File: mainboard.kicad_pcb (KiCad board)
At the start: 2 copper layers, 144 parts, among them IC1 ATXMEGA128A1U-A, J1 USB, K1 X_MIN, K2 X_MAX, K3 Y_MIN, K4 Y_MAX, K5 Z_MIN, K6 Z_MAX, P1 POWER, P10 USART, P11 TH_HB, P12 TH_EX, P13 TH_HO, P14 LCD, P15 STP_Y, P16 STP_E0, P17 STP_X, P18 STP_E1, P19 STP_Z, P2 PDI, P20 EXTR, P21 HIC_0, P22 HEATBED, P23 HIC_1, P24 FAN_0, P25 FAN_1, P26 LOC_0, P27 LOC_1, P28 INTERFACE, P3 GPIO_B, P4 BEEPER, P5 OPEN_COLL_D, P6 12V, P7 5V, P8 3.3V, P9 I2C, Q1 IRL1404, Q2 IRL1404, Q3 IRL1404, Q4 IRL1404, SW1 Y, SW2 E0, SW3 X, SW4 E1, SW5 Z, U1 NE 4558 D SMD, U10 ULN_2003_A, U2 ULN_2003_A, U3 A4988-BO, U4 A4988-BO, U5 A4988-BO, U6 A4988-BO, U7 A4988-BO, U8 MCP14E10, U9 MCP14E10

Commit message: * Changed order of stepper connections to UC to ease PCB routing * Arranged all items in 12x12cm space, ready to route(?)
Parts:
- C10, C11, C2, C4, C5, C6, C7, C8, C9, R1, R2, R21, R22, R23, R24: moved to B.Cu
- P1: footprint Connect:PINHEAD1-6 -> Connect:bornier6
- P11, P12, P13: footprint Connect:PINHEAD1-2 -> 3dp-special:PSS2
- moved P5 319.2 mm to (20.0, 109.5), turned to 270 degrees
- moved U2 308.8 mm to (30.5, 112.5), turned to 270 degrees
- moved C17 238.9 mm to (103.8, 42.8), turned to 90 degrees
- moved P14 230.0 mm to (109.8, 46.8), turned to 270 degrees
- moved R7 219.9 mm to (121.0, 40.5), turned to 90 degrees
- moved RV5 218.5 mm to (110.0, 28.5), turned to 270 degrees
- moved R26 215.6 mm to (48.0, 41.0), turned to 270 degrees
- moved R6 214.9 mm to (118.5, 47.0), turned to 90 degrees
- moved VR1 213.2 mm to (121.0, 46.5), turned to 90 degrees
- moved J1 209.0 mm to (126.5, 30.2), turned to 90 degrees
- moved VR2 209.0 mm to (118.5, 52.5), turned to 90 degrees
- moved R32 206.9 mm to (45.0, 75.0), turned to 90 degrees
- moved SW2 206.4 mm to (129.5, 45.0), turned to 90 degrees
- moved C12 205.1 mm to (121.5, 53.5), turned to 90 degrees
- moved R30 204.1 mm to (45.0, 86.0), turned to 90 degrees
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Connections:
- IC1 pad 56: Y-DIR -> X-STEP
- IC1 pad 57: Z-DIR -> X-EN
- IC1 pad 58: E0-STEP -> Y-DIR
- IC1 pad 59: E1-STEP -> Y-STEP
- IC1 pad 60: X-STEP -> Y-EN
- IC1 pad 61: Y-STEP -> Z-DIR
- IC1 pad 65: E0-EN -> Z-EN
- IC1 pad 66: E1-EN -> E0-DIR
- IC1 pad 67: X-EN -> E0-STEP
- IC1 pad 68: Y-EN -> E0-EN
- IC1 pad 69: Z-EN -> E1-DIR
- IC1 pad 70: E0-DIR -> E1-STEP
- IC1 pad 71: E1-DIR -> E1-EN
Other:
- board text added: "3V3"
- board text added: "E0"
- board text added: "E1"
- board text added: "GND"
- board text added: "HEATSINK"
- board text added: "SCL"
- board text added: "SDA"
- board text added: "STEP_X SETTINGS"
- board text added: "STEP_Y SETTINGS"
- board text added: "TH_EX"
- board text added: "TH_HB"
- board text added: "TH_HO"
- board text added: "VOL"
- board text added: "X"
- board text added: "Y"
- board text added: "Z"

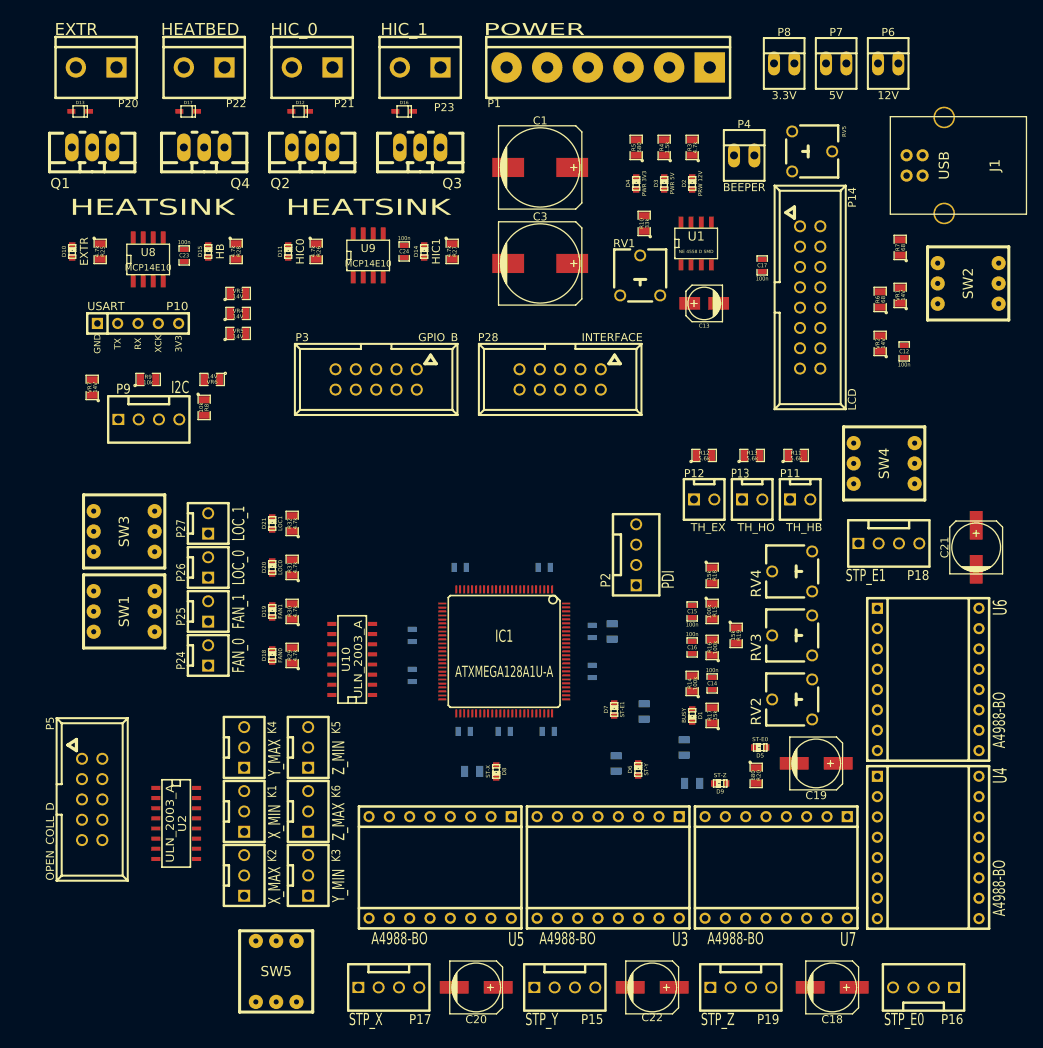
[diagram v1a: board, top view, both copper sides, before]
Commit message: * Schematic: Added decoupling cap for XMega * Schematic: Changed connector pin assignment for easier routing * Board: Changed arrangement of some components * Board: Routed all signal nets. To Do: Power nets.
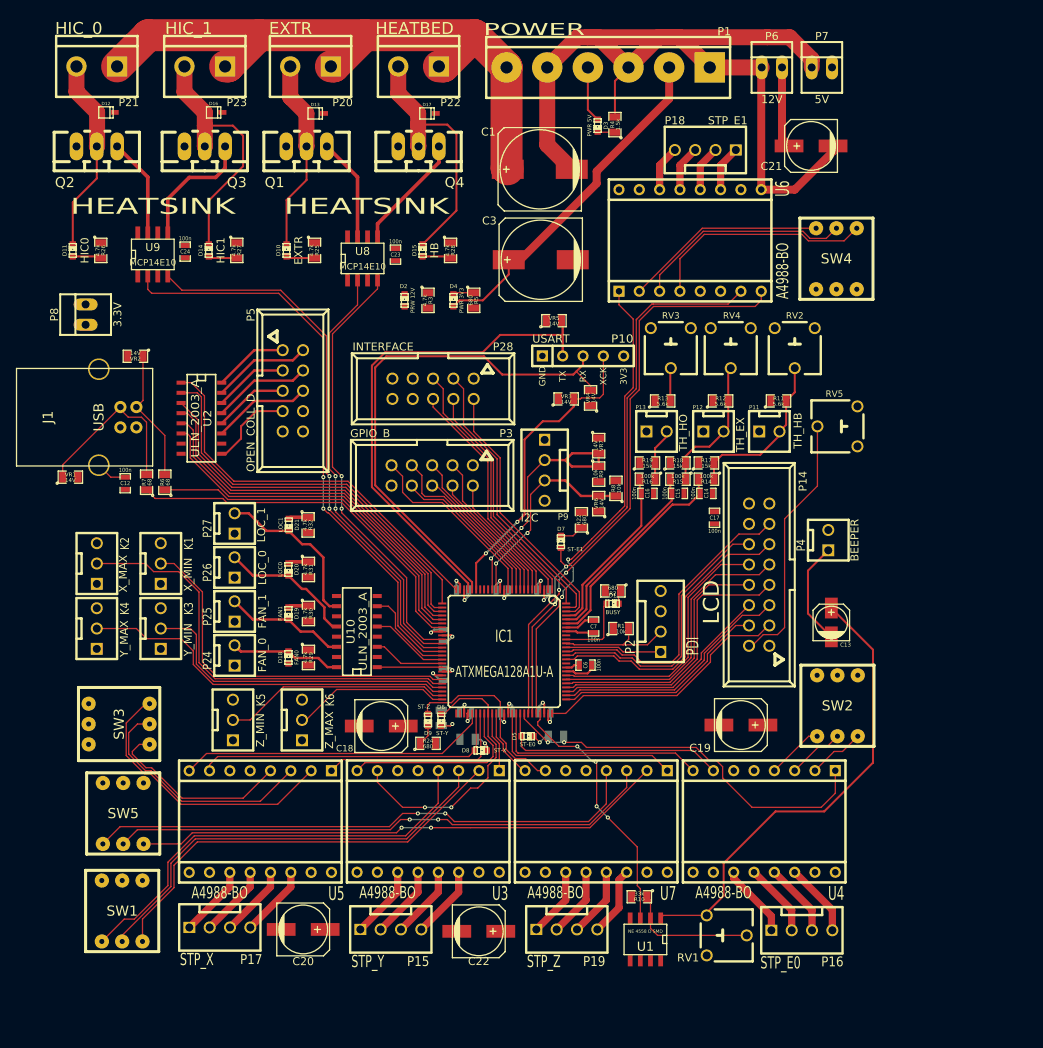
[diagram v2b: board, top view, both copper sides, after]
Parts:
- added C25: 100n, SMD_Packages:SM0603_Capa, B.Cu at (71.2, 83.3)
- C6, C7, R1, R2, R22, R24: moved to F.Cu
- P4: footprint Connect:PINHEAD1-2 -> 3dp-special:PSS2
- R20: moved to B.Cu
- moved J1 110.3 mm to (20.8, 61.7), turned to 270 degrees
- moved VR1 106.2 mm to (17.3, 69.2), turned to 0 degrees
- moved C12 98.8 mm to (24.1, 70.0), turned to 270 degrees
- moved R7 98.7 mm to (26.8, 69.8)
- moved VR2 93.1 mm to (25.4, 54.1), turned to 180 degrees
- moved P8 92.8 mm to (19.2, 48.9), turned to 90 degrees
- moved R6 92.3 mm to (29.1, 69.8)
- moved U1 87.2 mm to (89.2, 127.0), turned to 180 degrees
- moved R10 84.2 mm to (88.4, 121.7), turned to 180 degrees
- moved RV1 83.2 mm to (99.3, 126.5), turned to 270 degrees
- moved C18 65.1 mm to (56.1, 100.3)
- moved VR7 63.7 mm to (83.3, 65.3), turned to 270 degrees
- moved U6 62.4 mm to (94.7, 39.6), turned to 0 degrees
- moved R9 57.5 mm to (83.3, 68.8), turned to 270 degrees
- moved P5 56.9 mm to (45.1, 58.4)
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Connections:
- net Net-(D18-Pad2) renamed /heater-fan-driver/FAN1_OPEM
- net Net-(D19-Pad2) renamed /heater-fan-driver/FAN0_OPEM
- net Net-(D20-Pad2) renamed /heater-fan-driver/LOC1_OPEM
- net Net-(D21-Pad2) renamed /heater-fan-driver/LOC0_OPEM
- IC1 pad 17: /LCD_EN -> Net-(IC1-Pad17)
- IC1 pad 18: /LCD_RS -> Net-(IC1-Pad18)
- IC1 pad 86: Net-(IC1-Pad86) -> /LCD_RW
- IC1 pad 87: Net-(D1-Pad1) -> /LCD_RS
- IC1 pad 88: Net-(IC1-Pad88) -> /LCD_EN
- IC1 pad 91: Net-(IC1-Pad91) -> Net-(D1-Pad1)
- P14 pad 10: /LCD_D1 -> /LCD_D7
- P14 pad 11: /LCD_D0 -> /LCD_RW
- P14 pad 3: GND -> /LCD_D0
- P14 pad 4: /LCD_D7 -> /LCD_D1
- P14 pad 5: /LCD_D6 -> /LCD_D2
- P14 pad 6: /LCD_D5 -> /LCD_D3
- P14 pad 8: /LCD_D3 -> /LCD_D5
- P14 pad 9: /LCD_D2 -> /LCD_D6
- SW1 pad 1: Net-(SW1-Pad1) -> +3.3V
- SW1 pad 2: Net-(SW1-Pad2) -> +3.3V
- SW1 pad 3: Net-(SW1-Pad3) -> +3.3V
- SW1 pad 4: +3.3V -> Net-(SW1-Pad4)
- SW1 pad 5: +3.3V -> Net-(SW1-Pad5)
- SW1 pad 6: +3.3V -> Net-(SW1-Pad6)
- SW2 pad 1: Net-(SW2-Pad1) -> +3.3V
- SW2 pad 2: Net-(SW2-Pad2) -> +3.3V
- SW2 pad 3: Net-(SW2-Pad3) -> +3.3V
- SW2 pad 4: +3.3V -> Net-(SW2-Pad4)
- SW2 pad 5: +3.3V -> Net-(SW2-Pad5)
- SW2 pad 6: +3.3V -> Net-(SW2-Pad6)
- SW3 pad 1: Net-(SW3-Pad1) -> +3.3V
- SW3 pad 2: Net-(SW3-Pad2) -> +3.3V
- SW3 pad 3: Net-(SW3-Pad3) -> +3.3V
- SW3 pad 4: +3.3V -> Net-(SW3-Pad4)
- SW3 pad 5: +3.3V -> Net-(SW3-Pad5)
- SW3 pad 6: +3.3V -> Net-(SW3-Pad6)
- SW4 pad 1: Net-(SW4-Pad1) -> +3.3V
- SW4 pad 2: Net-(SW4-Pad2) -> +3.3V
- SW4 pad 3: Net-(SW4-Pad3) -> +3.3V
- SW4 pad 4: +3.3V -> Net-(SW4-Pad4)
- SW4 pad 5: +3.3V -> Net-(SW4-Pad5)
- SW4 pad 6: +3.3V -> Net-(SW4-Pad6)
- SW5 pad 1: Net-(SW5-Pad1) -> +3.3V
- SW5 pad 2: Net-(SW5-Pad2) -> +3.3V
- SW5 pad 3: Net-(SW5-Pad3) -> +3.3V
- SW5 pad 4: +3.3V -> Net-(SW5-Pad4)
- SW5 pad 5: +3.3V -> Net-(SW5-Pad5)
- SW5 pad 6: +3.3V -> Net-(SW5-Pad6)
- U10 pad 1: /heater-fan-driver/IN_FAN_0 -> /heater-fan-driver/IN_FAN_1
- U10 pad 3: /heater-fan-driver/IN_FAN_1 -> /heater-fan-driver/IN_FAN_0
- U10 pad 5: /heater-fan-driver/IN_LOC_0 -> /heater-fan-driver/IN_LOC_1
- U10 pad 7: /heater-fan-driver/IN_LOC_1 -> /heater-fan-driver/IN_LOC_0
- U3 pad 2: Net-(SW1-Pad3) -> Net-(SW1-Pad6)
- U3 pad 3: Net-(SW1-Pad2) -> Net-(SW1-Pad5)
- U3 pad 4: Net-(SW1-Pad1) -> Net-(SW1-Pad4)
- U4 pad 2: Net-(SW2-Pad3) -> Net-(SW2-Pad6)
- U4 pad 3: Net-(SW2-Pad2) -> Net-(SW2-Pad5)
- U4 pad 4: Net-(SW2-Pad1) -> Net-(SW2-Pad4)
- U5 pad 2: Net-(SW3-Pad3) -> Net-(SW3-Pad6)
- U5 pad 3: Net-(SW3-Pad2) -> Net-(SW3-Pad5)
- U5 pad 4: Net-(SW3-Pad1) -> Net-(SW3-Pad4)
- U6 pad 2: Net-(SW4-Pad3) -> Net-(SW4-Pad6)
- U6 pad 3: Net-(SW4-Pad2) -> Net-(SW4-Pad5)
- U6 pad 4: Net-(SW4-Pad1) -> Net-(SW4-Pad4)
- U7 pad 2: Net-(SW5-Pad3) -> Net-(SW5-Pad6)
- U7 pad 3: Net-(SW5-Pad2) -> Net-(SW5-Pad5)
- U7 pad 4: Net-(SW5-Pad1) -> Net-(SW5-Pad4)
- U8 pad 2: /heater-fan-driver/IN_EXTR -> /heater-fan-driver/IN_HEATBED
- U8 pad 4: /heater-fan-driver/IN_HEATBED -> /heater-fan-driver/IN_EXTR
- U9 pad 2: /heater-fan-driver/IN_HIC_0 -> /heater-fan-driver/IN_HIC_1
- U9 pad 4: /heater-fan-driver/IN_HIC_1 -> /heater-fan-driver/IN_HIC_0
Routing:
- net GND: track 0.00 -> 138.2 mm, vias 0 -> 8
- net +12V: track 0.00 -> 93.0 mm
- net /heater-fan-driver/IN_HIC_1: track 0.00 -> 72.9 mm, vias 0 -> 2
- net +3.3V: track 0.00 -> 72.7 mm, vias 0 -> 8
- net E1-DIR: track 0.00 -> 72.6 mm, vias 0 -> 2
- net E1-STEP: track 0.00 -> 71.9 mm, vias 0 -> 2
- net Net-(SW5-Pad4): track 0.00 -> 70.0 mm, vias 0 -> 2
- net /heater-fan-driver/IN_HIC_0: track 0.00 -> 69.2 mm, vias 0 -> 2
- net Net-(SW5-Pad5): track 0.00 -> 68.5 mm, vias 0 -> 2
- net Net-(SW5-Pad6): track 0.00 -> 66.7 mm, vias 0 -> 2
- net /USARTC1-RXD1: track 0.00 -> 65.0 mm
- net /USARTC1-TXD1: track 0.00 -> 63.1 mm
- net E1-EN: track 0.00 -> 59.3 mm, vias 0 -> 2
- net Net-(C13-Pad1): track 0.00 -> 58.7 mm
- net Net-(SW1-Pad4): track 0.00 -> 55.0 mm
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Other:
- net class Default: clearance 0.254 -> 0.1524; via_dia 0.889 -> 0.508; via_drill 0.635 -> 0.3302
- net class Signal added: clearance 0.1524, trace_width 0.1524, via_dia 0.508, via_drill 0.3302
- rule trace_clearance: 0.254 -> 0.1524
- rule trace_min: 0.254 -> 0.1524
- rule via_min_drill: 0.508 -> 0.3302
- rule via_min_size: 0.889 -> 0.508
- board text added: "12V"
- board text added: "5V"
- board text added: "LCD Contrast"
- board text added: "Mainboard"
- board text added: "Philipp Neininger Manuel Kuttruff"
- board text added: "QsP"
- board text added: "STEP_E0"
- board text added: "STEP_E1"
- board text added: "STEP_X"
- board text added: "STEP_Y"
- board text added: "STEP_Z"
- board text removed: "STEP_X SETTINGS"
- board text removed: "STEP_Y SETTINGS"

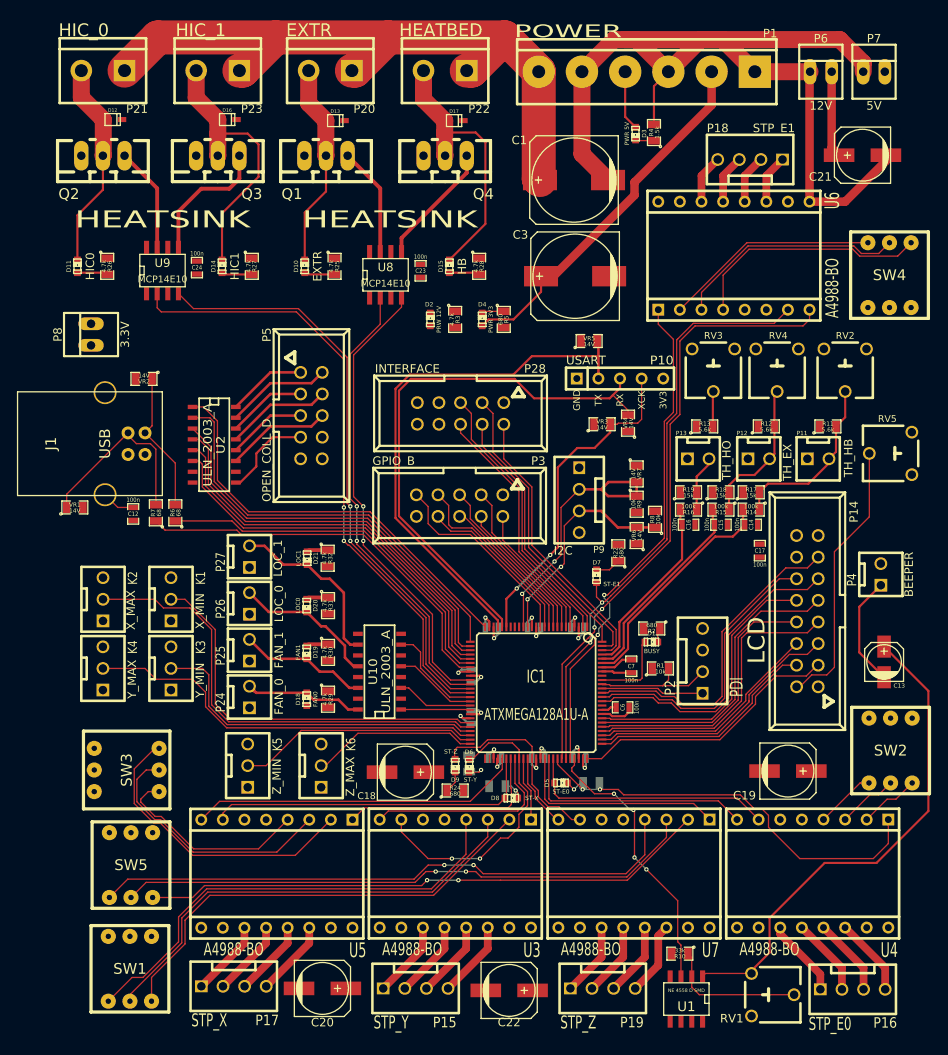
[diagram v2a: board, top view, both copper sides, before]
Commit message: Router parts of the power layer
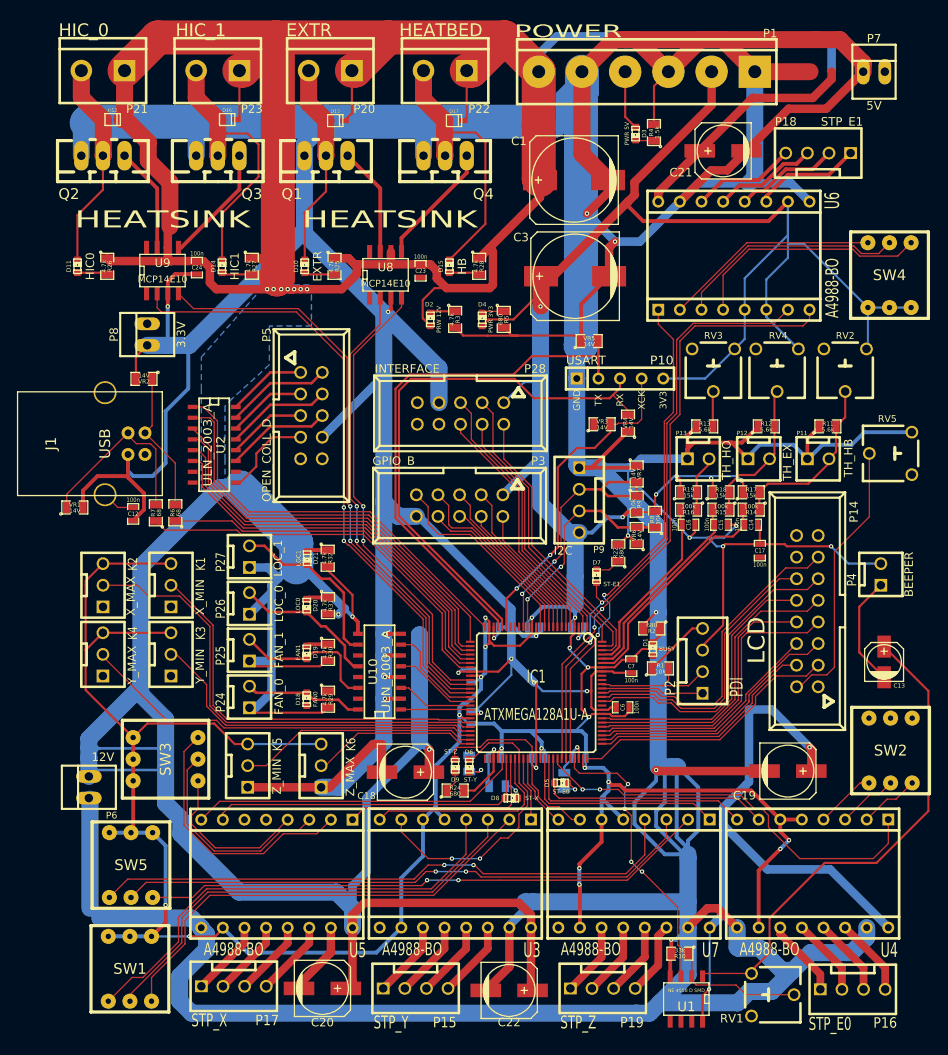
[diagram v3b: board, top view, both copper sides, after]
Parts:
- moved P6 120.3 mm to (18.9, 102.1), turned to 90 degrees
- moved C21 16.4 mm to (93.5, 27.3)
- moved P18 8.04 mm to (109.7, 27.6)
- moved P8 6.60 mm to (25.8, 48.9)
- moved SW3 4.75 mm to (27.9, 98.8)
- moved R20 3.19 mm to (74.8, 101.3), turned to 90 degrees
- moved K1 1.65 mm to (28.6, 78.4)
- moved K3 1.65 mm to (28.6, 86.5)
- moved K4 1.65 mm to (20.6, 86.5)
- moved K2 1.65 mm to (20.6, 78.4)
- moved D1 0.84 mm to (85.2, 85.9), turned to 90 degrees
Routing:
- net GND: track 138.2 -> 1105.3 mm, vias 8 -> 27
- net +12V: track 93.0 -> 665.2 mm, vias 0 -> 12
- net +3.3V: track 72.7 -> 563.6 mm, vias 8 -> 25
- net Net-(D1-Pad1): track 9.48 -> 0.00 mm
- net /motortreiber-sub/E11B: track 5.74 -> 12.6 mm
- net /motortreiber-sub/E12B: track 5.74 -> 12.5 mm
- net /motortreiber-sub/E11A: track 5.74 -> 12.3 mm
- net /motortreiber-sub/E12A: track 5.74 -> 12.3 mm
- net Net-(SW3-Pad5): track 30.0 -> 25.3 mm
- net Net-(SW3-Pad4): track 23.8 -> 19.2 mm
- net Net-(SW3-Pad6): track 35.4 -> 31.3 mm
- net Net-(D2-Pad2): track 0.00 -> 3.01 mm
- net /heater-fan-driver/FAN0_OPEM: track 15.1 -> 17.5 mm
- net Net-(Q3-PadG): track 15.7 -> 14.0 mm
- net /BEEPER: track 32.6 -> 33.8 mm
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- added copper zone on B.Cu, net +12V
